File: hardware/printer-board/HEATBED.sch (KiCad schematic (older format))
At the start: 7 parts, among them J23 HEATBED, Q1 WSK220N04

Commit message: update,
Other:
- moved on the sheet: D3, J23, R26
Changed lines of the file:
@@
 L Connector:Screw_Terminal_01x02 J23
 U 1 1 5CC0B91A
-P 5250 2900
+P 5250 2700
 AR Path="/5CC0B758/5CC0B91A" Ref="J23"  Part="1"
 AR Path="/5CC12903/5CC0B91A" Ref="J?"  Part="1"
 AR Path="/5CC1B272/5CC0B91A" Ref="J?"  Part="1"
 AR Path="/5CC1F2C3/5CC0B91A" Ref="J?"  Part="1"
-F 0 "J23" H 5169 2575 50  0000 C CNN
-F 1 "HEATBED" H 5169 2666 50  0000 C CNN
-F 2 "footprint-lib:mpt_0,5%2f2-2,54,heatbed" H 5250 2900 50  0001 C CNN
-F 3 "~" H 5250 2900 50  0001 C CNN
-	1    5250 2900
-	1    0    0    1
+F 0 "J23" H 5169 2375 50  0000 C CNN
+F 1 "HEATBED" H 5169 2466 50  0000 C CNN
+F 2 "footprint-lib:mpt_0,5%2f2-2,54,heatbed" H 5250 2700 50  0001 C CNN
+F 3 "~" H 5250 2700 50  0001 C CNN
+	1    5250 2700
+	1    0    0    -1
 $EndComp
 $Comp
@@
 L taobao-r:R182,0603 R26
 U 1 1 5CC0C120
-P 4050 3350
+P 4050 2250
 AR Path="/5CC0B758/5CC0C120" Ref="R26"  Part="1"
 AR Path="/5CC12903/5CC0C120" Ref="R?"  Part="1"
 AR Path="/5CC1B272/5CC0C120" Ref="R?"  Part="1"
 AR Path="/5CC1F2C3/5CC0C120" Ref="R?"  Part="1"
-F 0 "R26" H 4109 3396 50  0000 L CNN
-F 1 "R182,0603" H 4109 3305 50  0000 L CNN
-F 2 "Resistor_SMD:R_0603_1608Metric_Pad1.05x0.95mm_HandSolder" H 4050 3350 50  0001 C CNN
-F 3 "~" H 4050 3350 50  0001 C CNN
-	1    4050 3350
-	1    0    0    -1
+F 0 "R26" H 4109 2296 50  0000 L CNN
+F 1 "R182,0603" H 4109 2205 50  0000 L CNN
+F 2 "Resistor_SMD:R_0603_1608Metric_Pad1.05x0.95mm_HandSolder" H 4050 2250 50  0001 C CNN
+F 3 "~" H 4050 2250 50  0001 C CNN
+	1    4050 2250
+	1    0    0    1
 $EndComp
 $Comp
 L taobao-led:LED_RED,0603 D3
 U 1 1 5CC0C24D
-P 4050 3050
+P 4050 2550
 AR Path="/5CC0B758/5CC0C24D" Ref="D3"  Part="1"
 AR Path="/5CC12903/5CC0C24D" Ref="D?"  Part="1"
 AR Path="/5CC1B272/5CC0C24D" Ref="D?"  Part="1"
 AR Path="/5CC1F2C3/5CC0C24D" Ref="D?"  Part="1"
-F 0 "D3" V 4004 3148 50  0000 L CNN
-F 1 "LED_RED,0603" V 4095 3148 50  0000 L CNN
-F 2 "LED_SMD:LED_0603_1608Metric_Pad1.05x0.95mm_HandSolder" V 4050 3050 50  0001 C CNN
-F 3 "" V 4050 3050 50  0001 C CNN
-	1    4050 3050
-	0    1    1    0
+F 0 "D3" V 4004 2648 50  0000 L CNN
+F 1 "LED_RED,0603" V 4095 2648 50  0000 L CNN
+F 2 "LED_SMD:LED_0603_1608Metric_Pad1.05x0.95mm_HandSolder" V 4050 2550 50  0001 C CNN
+F 3 "" V 4050 2550 50  0001 C CNN
+	1    4050 2550
+	0    1    -1   0
 $EndComp
 Wire Wire Line
@@
 	3200 2800 3200 2900
 Wire Wire Line
-	4050 2950 4050 2800
+	4050 2650 4050 2800
 Connection ~ 4050 2800
 Wire Wire Line
 	4050 2800 3200 2800
 Wire Wire Line
-	4050 3150 4050 3250
+	4050 2450 4050 2350
 $Comp
 L taobao-components:+12V2 #PWR0226
 U 1 1 5CC10EF1
-P 4750 2900
+P 4750 1900
 AR Path="/5CC0B758/5CC10EF1" Ref="#PWR0226"  Part="1"
 AR Path="/5CC12903/5CC10EF1" Ref="#PWR?"  Part="1"
 AR Path="/5CC1B272/5CC10EF1" Ref="#PWR?"  Part="1"
 AR Path="/5CC1F2C3/5CC10EF1" Ref="#PWR?"  Part="1"
-F 0 "#PWR0226" H 4750 2750 50  0001 C CNN
-F 1 "+12V2" V 4765 3028 50  0000 L CNN
-F 2 "" H 4750 2900 50  0001 C CNN
-F 3 "" H 4750 2900 50  0001 C CNN
-	1    4750 2900
-	0    -1   -1   0
+F 0 "#PWR0226" H 4750 1750 50  0001 C CNN
+F 1 "+12V2" V 4765 2028 50  0000 L CNN
+F 2 "" H 4750 1900 50  0001 C CNN
+F 3 "" H 4750 1900 50  0001 C CNN
+	1    4750 1900
+	-1   0    0    -1
 $EndComp
 Wire Wire Line
-	5050 2900 4900 2900
+	5050 2700 4900 2700
 Wire Wire Line
-	4900 2900 4900 3550
+	4900 2700 4900 2050
 Wire Wire Line
-	4900 3550 4050 3550
-Wire Wire Line
-	4050 3550 4050 3450
-Connection ~ 4900 2900
-Wire Wire Line
-	4900 2900 4750 2900
+	4050 2050 4050 2150
 Text HLabel 1250 900  0    50   Input ~ 0
 HEATBED_EN
@@
 EndData
 $EndBitmap
+Wire Wire Line
+	4750 1900 4750 2050
+Wire Wire Line
+	4050 2050 4750 2050
+Connection ~ 4750 2050
+Wire Wire Line
+	4750 2050 4900 2050
 $EndSCHEMATC

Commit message: update,
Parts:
- removed C26: CP100uf,16V, Capacitor_SMD:CP_Elec_6.3x5.3, symbol taobao-cp:CP100uf,16V
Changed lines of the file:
@@
 Wire Wire Line
 	1950 3100 2350 3100
-$Comp
-L taobao-components:+12V2 #PWR0227
-U 1 1 5CC148B0
-P 2550 4200
-AR Path="/5CC0B758/5CC148B0" Ref="#PWR0227"  Part="1"
-AR Path="/5CC12903/5CC148B0" Ref="#PWR?"  Part="1"
-AR Path="/5CC1B272/5CC148B0" Ref="#PWR?"  Part="1"
-AR Path="/5CC1F2C3/5CC148B0" Ref="#PWR?"  Part="1"
-F 0 "#PWR0227" H 2550 4050 50  0001 C CNN
-F 1 "+12V2" V 2565 4328 50  0000 L CNN
-F 2 "" H 2550 4200 50  0001 C CNN
-F 3 "" H 2550 4200 50  0001 C CNN
-	1    2550 4200
-	0    -1   -1   0
-$EndComp
-$Comp
-L power:GND #PWR0228
-U 1 1 5CC148C7
-P 3200 4200
-AR Path="/5CC0B758/5CC148C7" Ref="#PWR0228"  Part="1"
-AR Path="/5CC12903/5CC148C7" Ref="#PWR?"  Part="1"
-AR Path="/5CC1B272/5CC148C7" Ref="#PWR?"  Part="1"
-AR Path="/5CC1F2C3/5CC148C7" Ref="#PWR?"  Part="1"
-F 0 "#PWR0228" H 3200 3950 50  0001 C CNN
-F 1 "GND" V 3205 4072 50  0000 R CNN
-F 2 "" H 3200 4200 50  0001 C CNN
-F 3 "" H 3200 4200 50  0001 C CNN
-	1    3200 4200
-	0    -1   -1   0
-$EndComp
-$Comp
-L taobao-cp:CP100uf,16V C26
-U 1 1 5CC14A08
-P 2850 4200
-AR Path="/5CC0B758/5CC14A08" Ref="C26"  Part="1"
-AR Path="/5CC1B272/5CC14A08" Ref="C?"  Part="1"
-AR Path="/5CC1F2C3/5CC14A08" Ref="C?"  Part="1"
-F 0 "C26" V 3075 4200 50  0000 C CNN
-F 1 "CP100uf,16V" V 2984 4200 50  0000 C CNN
-F 2 "Capacitor_SMD:CP_Elec_6.3x5.3" H 2850 4200 50  0001 C CNN
-F 3 "~" H 2850 4200 50  0001 C CNN
-	1    2850 4200
-	0    -1   -1   0
-$EndComp
-Wire Wire Line
-	2550 4200 2750 4200
-Wire Wire Line
-	2950 4200 3200 4200
 $Bitmap
 Pos 9450 5000

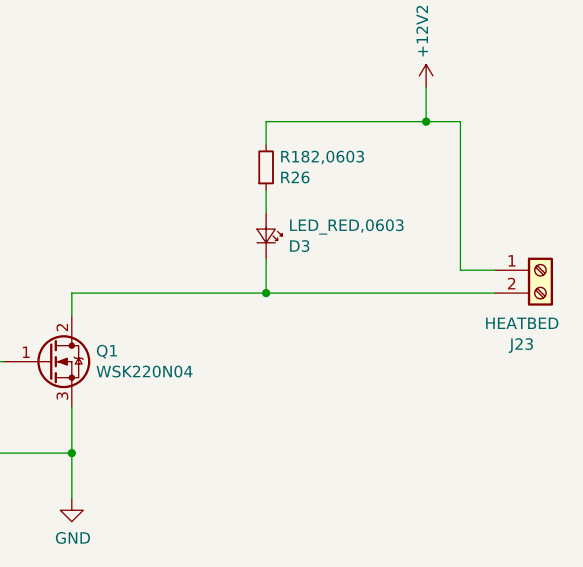
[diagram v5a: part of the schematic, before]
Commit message: update heatbed,
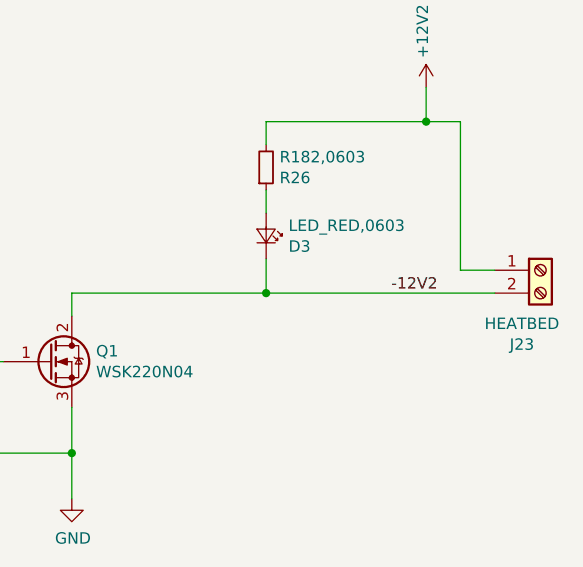
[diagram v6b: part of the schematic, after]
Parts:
- Q1: footprint Package_TO_SOT_SMD:TO-263-2 -> footprint-lib:TO-263-2,drill_array
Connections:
- net -12V2: now reaches D3.1 (K), J23.2 (Pin_2), Q1.2 (D)
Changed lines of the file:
@@
 EESchema Schematic File Version 4
-LIBS:printer-board-cache
 EELAYER 26 0
 EELAYER END
 $Descr A4 11693 8268
 encoding utf-8
-Sheet 10 32
+Sheet 1 1
 Title ""
 Date ""
@@
 AR Path="/5CC1B272/5CC0B91A" Ref="J?"  Part="1"
 AR Path="/5CC1F2C3/5CC0B91A" Ref="J?"  Part="1"
+AR Path="/5CC0B91A" Ref="J23"  Part="1"
 F 0 "J23" H 5169 2375 50  0000 C CNN
 F 1 "HEATBED" H 5169 2466 50  0000 C CNN
@@
 AR Path="/5CC1B272/5CC0BC7B" Ref="Q?"  Part="1"
 AR Path="/5CC1F2C3/5CC0BC7B" Ref="Q?"  Part="1"
+AR Path="/5CC0BC7B" Ref="Q1"  Part="1"
 F 0 "Q1" H 3306 3146 50  0000 L CNN
 F 1 "WSK220N04" H 3306 3055 50  0000 L CNN
-F 2 "Package_TO_SOT_SMD:TO-263-2" H 3300 3200 50  0001 C CNN
+F 2 "footprint-lib:TO-263-2,drill_array" H 3300 3200 50  0001 C CNN
 F 3 "~" H 3100 3100 50  0001 C CNN
 	1    3100 3100
@@
 AR Path="/5CC1B272/5CC0BDB8" Ref="R?"  Part="1"
 AR Path="/5CC1F2C3/5CC0BDB8" Ref="R?"  Part="1"
+AR Path="/5CC0BDB8" Ref="R24"  Part="1"
 F 0 "R24" V 2254 3100 50  0000 C CNN
 F 1 "R100,0805" V 2345 3100 50  0000 C CNN
@@
 AR Path="/5CC1B272/5CC0BF5E" Ref="R?"  Part="1"
 AR Path="/5CC1F2C3/5CC0BF5E" Ref="R?"  Part="1"
+AR Path="/5CC0BF5E" Ref="R25"  Part="1"
 F 0 "R25" V 2254 3500 50  0000 C CNN
 F 1 "R104,0805" V 2345 3500 50  0000 C CNN
@@
 AR Path="/5CC1B272/5CC04D62" Ref="#PWR?"  Part="1"
 AR Path="/5CC1F2C3/5CC04D62" Ref="#PWR?"  Part="1"
+AR Path="/5CC04D62" Ref="#PWR0225"  Part="1"
 F 0 "#PWR0225" H 3200 3450 50  0001 C CNN
 F 1 "GND" H 3205 3527 50  0000 C CNN
@@
 AR Path="/5CC1B272/5CC0C120" Ref="R?"  Part="1"
 AR Path="/5CC1F2C3/5CC0C120" Ref="R?"  Part="1"
+AR Path="/5CC0C120" Ref="R26"  Part="1"
 F 0 "R26" H 4109 2296 50  0000 L CNN
 F 1 "R182,0603" H 4109 2205 50  0000 L CNN
@@
 AR Path="/5CC1B272/5CC0C24D" Ref="D?"  Part="1"
 AR Path="/5CC1F2C3/5CC0C24D" Ref="D?"  Part="1"
+AR Path="/5CC0C24D" Ref="D3"  Part="1"
 F 0 "D3" V 4004 2648 50  0000 L CNN
 F 1 "LED_RED,0603" V 4095 2648 50  0000 L CNN
@@
 AR Path="/5CC1B272/5CC10EF1" Ref="#PWR?"  Part="1"
 AR Path="/5CC1F2C3/5CC10EF1" Ref="#PWR?"  Part="1"
+AR Path="/5CC10EF1" Ref="#PWR0226"  Part="1"
 F 0 "#PWR0226" H 4750 1750 50  0001 C CNN
 F 1 "+12V2" V 4765 2028 50  0000 L CNN
@@
 Wire Wire Line
 	4750 2050 4900 2050
+Text Label 4800 2800 2    50   ~ 0
+-12V2
 $EndSCHEMATC
